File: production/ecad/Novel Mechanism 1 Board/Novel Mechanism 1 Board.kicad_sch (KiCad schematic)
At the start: 35 parts, among them U1 ADC081C021CIMM/NOPB, U2 ADC081C021CIMM/NOPB, U3 ADC081C021CIMM/NOPB

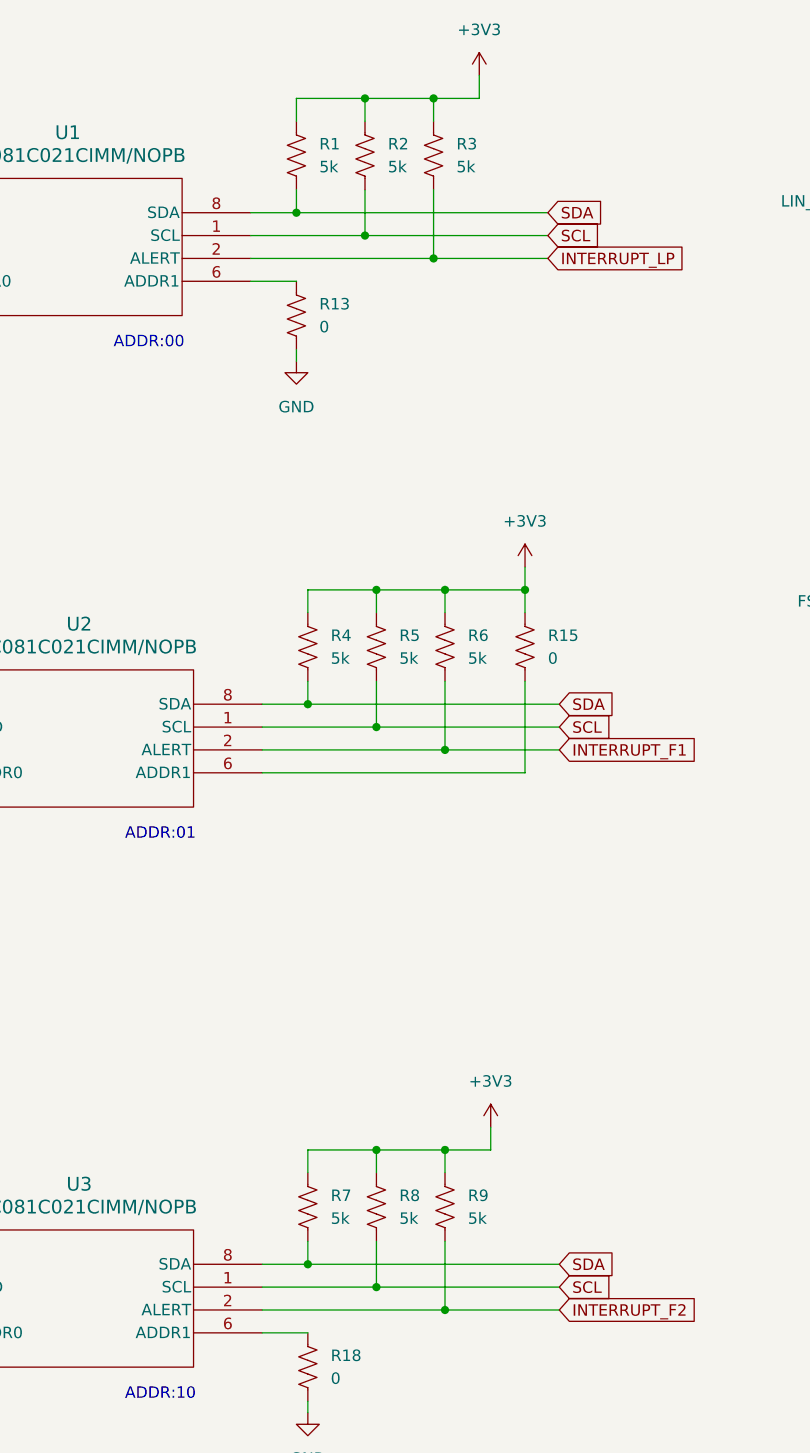
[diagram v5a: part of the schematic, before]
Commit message: NM1 Schematic Update
Updated footprints, added footprints to passives, modified some datasheets
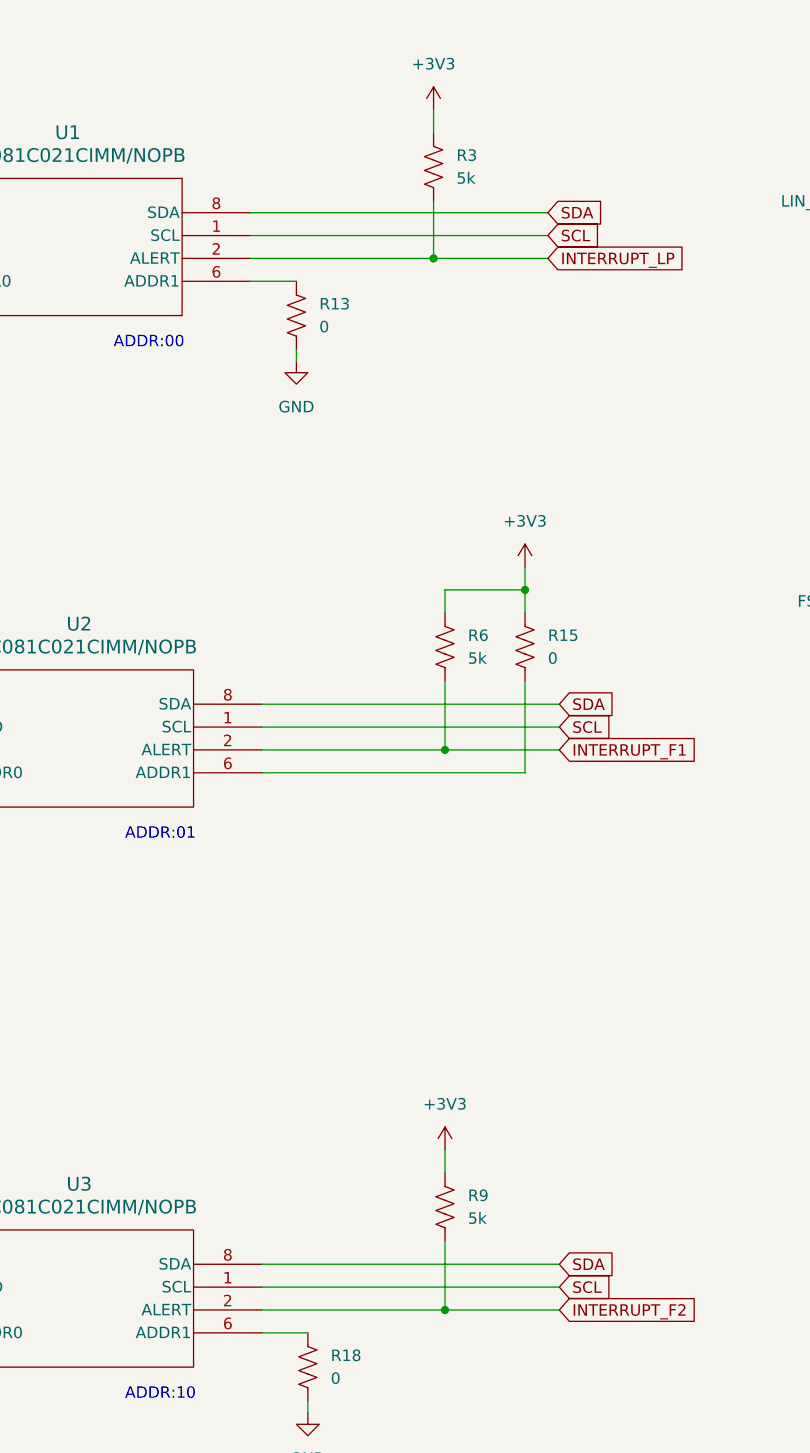
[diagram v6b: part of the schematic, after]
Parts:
- removed R1, R2, R4, R5, R7, R8: 5k, symbol Device:R_US
- C1, C2, C3, C4, C5, C6, C7, C8, C9: footprint (none) -> Capacitor_SMD:C_0402_1005Metric
- R10, R11, R12, R13, R14, R15, R16, R17, R18, R3, R6, R9: footprint (none) -> Resistor_SMD:R_0402_1005Metric
- U1, U2, U3: footprint Package_TO_SOT_SMD:SOT-23-8 -> Sensify:NM-ADC8BIT
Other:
- moved on the sheet: R3

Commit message: Footprints and Lables
modified input/output labels, modified footprint libraries. Sensify Footprints now points to the general footprint library that all of us have been tossing footprints into
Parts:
- U1, U2, U3: footprint Sensify:NM-ADC8BIT -> Sensify Footprints:NM-ADC8BIT
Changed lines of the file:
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@@
       (effects (font (size 1.524 1.524)))
     )
-    (property "Footprint" "Sensify:NM-ADC8BIT" (at 76.2 40.64 0)
+    (property "Footprint" "Sensify Footprints:NM-ADC8BIT" (at 76.2 40.64 0)
       (effects (font (size 1.27 1.27) italic) hide)
     )
@@
       (effects (font (size 1.524 1.524)))
     )
-    (property "Footprint" "Sensify:NM-ADC8BIT" (at 77.47 95.25 0)
+    (property "Footprint" "Sensify Footprints:NM-ADC8BIT" (at 77.47 95.25 0)
       (effects (font (size 1.27 1.27) italic) hide)
     )
@@
       (effects (font (size 1.524 1.524)))
     )
-    (property "Footprint" "Sensify:NM-ADC8BIT" (at 77.47 157.48 0)
+    (property "Footprint" "Sensify Footprints:NM-ADC8BIT" (at 77.47 157.48 0)
       (effects (font (size 1.27 1.27) italic) hide)
     )

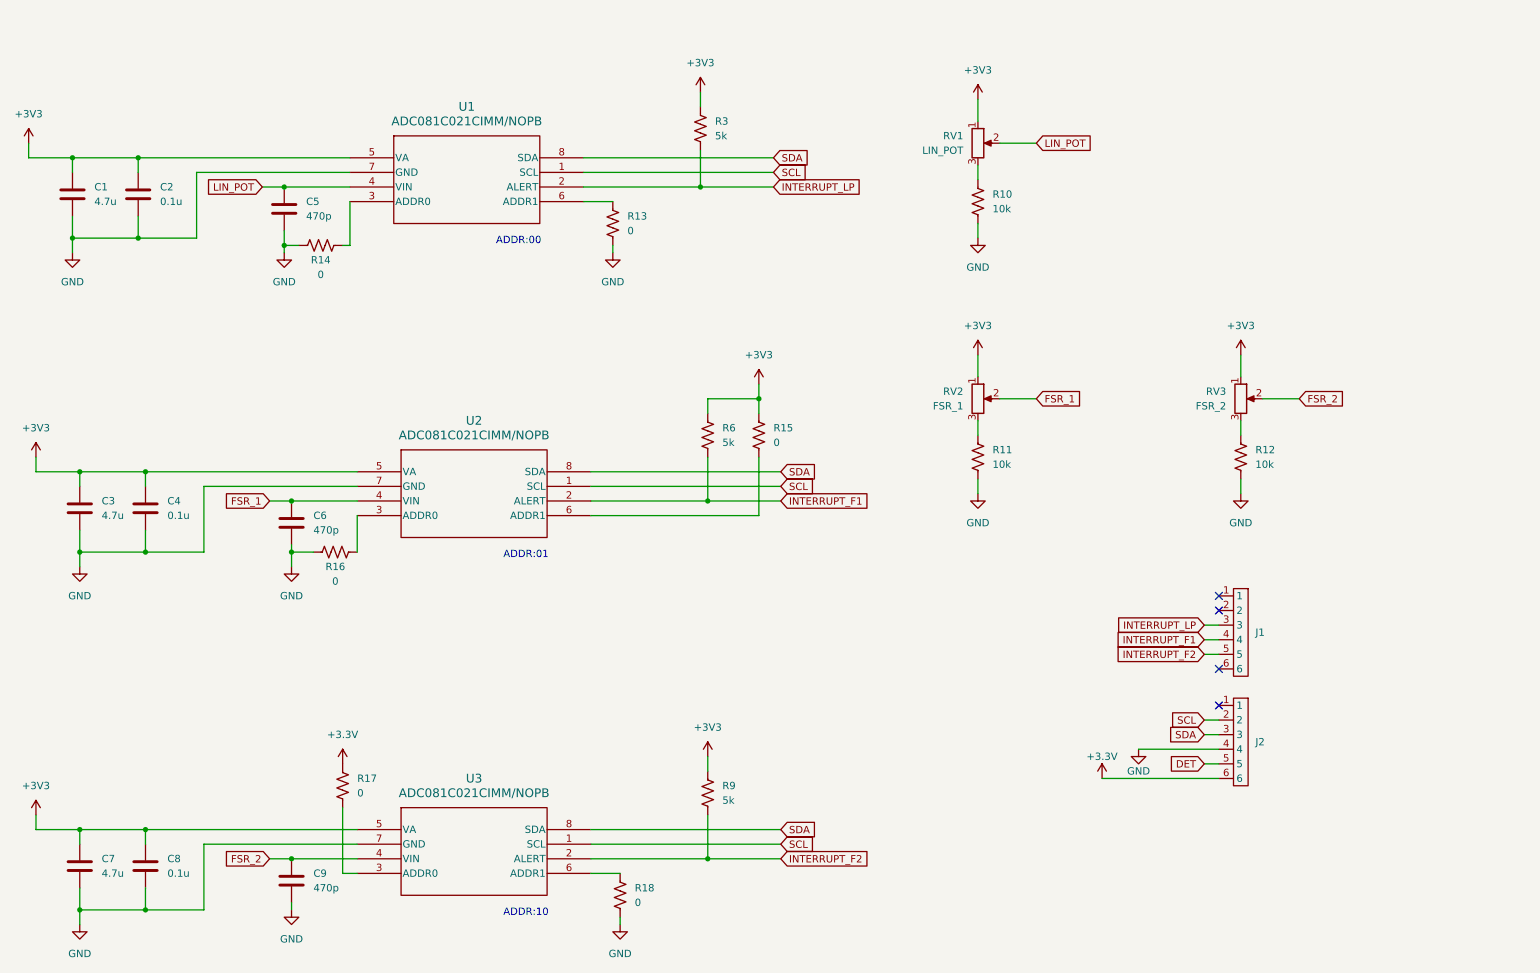
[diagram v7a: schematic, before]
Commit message: connector and labels
updated i/o net labels, added connector from MCU schematic
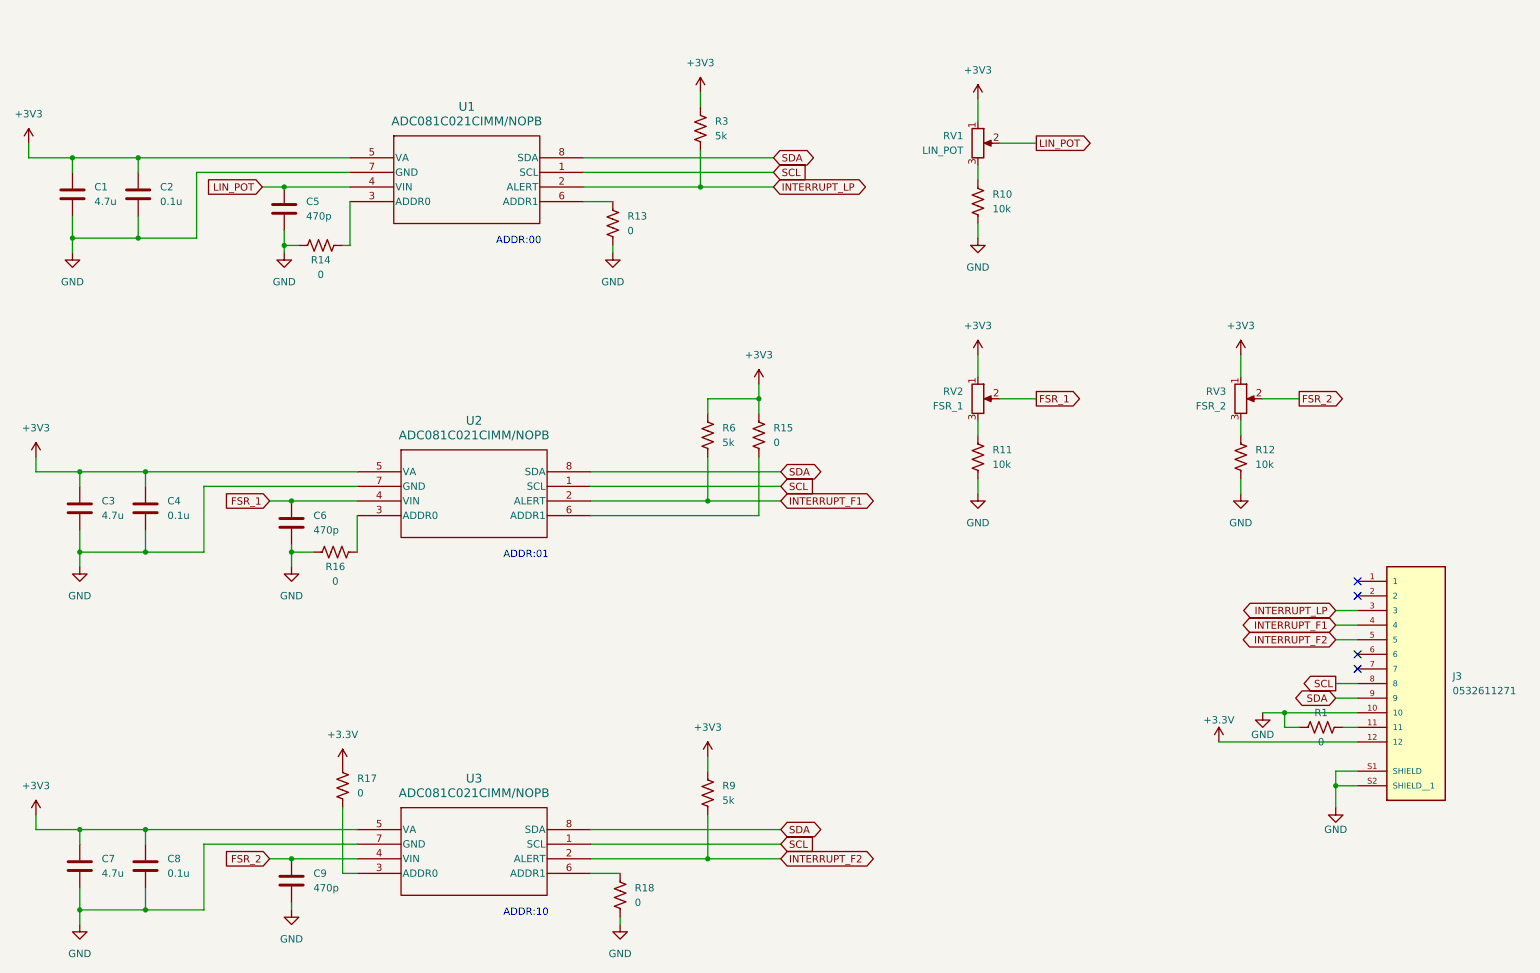
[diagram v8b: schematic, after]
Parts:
- removed J1, J2: ~, symbol ViseADC:6PIN_CONN
- added J3: 0532611271, Sensify Footprints:MOLEX_0532611271, symbol 0532611271:0532611271
- added R1: 0, Resistor_SMD:R_0402_1005Metric, symbol Device:R_US
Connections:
- net +3.3V: now also J3.12
- net GND: now also J3.10, J3.S1 (SHIELD), J3.S2 (SHIELD__1), R1.1
- net INTERRUPT_F1: now also J3.4
- net INTERRUPT_F2: now also J3.5
- net INTERRUPT_LP: now also J3.3
- net SCL: now also J3.8
- net SDA: now also J3.9
- new net: J3.11, R1.2
